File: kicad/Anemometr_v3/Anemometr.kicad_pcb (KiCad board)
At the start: 2 copper layers, 45 x 45 mm, 170 parts, among them J1 TxD, J10 +Z1, J11 +Z2, J12 +Z3, J13 +Z4, J14 -Z1, J15 -Z2, J16 -Z3, J17 -Z4, J18 1 TxD+, J19 2 TxD-, J2 RxD, J20 3 RxD+, J21 4-5, J22 6 RxD-, J23 7-8, J24 Conn_01x01_Female, J25 Conn_01x01_Female, J26 Conn_01x01_Female, J3 SCL, J4 SDA, J5 RST, J6 +EXT, J7 -EXT, J8 SWD, J9 SWC, Q1 5N10, U1 STM32F103C8Tx, U2 TS5A3166DBVR, U3 TS5A3166DBVR, U4 LMR14206, U5 TS5A3166DBVR, U6 NCP1117-3.3, U7 TS5A3166DBVR, U8 MCP1703-3.3, U9 MCP1703-3.3, Y1 CSTCE8M00G52A-R0, Y2 ECS-250-20-33

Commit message: изменено:      kicad/Anemometr_v3/Anemometr-cache.lib 	изменено:      kicad/Anemometr_v3/Anemometr.kicad_pcb 	изменено:      kicad/Anemometr_v3/Anemometr.kicad_pcb-bak 	изменено:      kicad/Anemometr_v3/Anemometr.sch 	изменено:      kicad/Anemometr_v3/Anemometr.sch-bak
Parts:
- removed C1, C17, C2, C21, C32, C5, C51, C52, C57, C59: 0.1uF, Capacitor_SMD:C_0402_1005Metric
- removed C18, C6: 10nF, Capacitor_SMD:C_0402_1005Metric
- removed C34, C40: 100nF, Capacitor_SMD:C_0402_1005Metric
- removed C41, C47: 1,5nF, Capacitor_SMD:C_0402_1005Metric
- removed C60, C61: 10uF, Capacitor_SMD:C_0805_2012Metric
- removed D19, D7: MAX4477, Package_SO:MSOP-8_3x3mm_P0.65mm
- removed D20, D21: TLV3501, Package_TO_SOT_SMD:SOT-23-6
- removed R13, R31: 20k, Resistor_SMD:R_0402_1005Metric
- removed R16, R25, R33, R46, R48, R50: 100k, Resistor_SMD:R_0402_1005Metric
- removed R17: 110k, Resistor_SMD:R_0402_1005Metric
- removed R20, R45: 1k, Resistor_SMD:R_0402_1005Metric
- removed R29, R47: 5.1k, Resistor_SMD:R_0402_1005Metric
- removed R37, R49: 10k, Resistor_SMD:R_0402_1005Metric
- removed R5, R51: 3k, Resistor_SMD:R_0402_1005Metric
- removed R6, R7, R8: 3k, Resistor_SMD:R_0603_1608Metric
- removed U2, U3, U5, U7: TS5A3166DBVR, Package_TO_SOT_SMD:SOT-23-5
- removed U8: MCP1703-3.3, Package_TO_SOT_SMD:SOT-23
- added J27: +Z1, My-library:SMD-CONN, F.Cu at (33.8, 64.5)
- added J28: +Z1, My-library:SMD-CONN, F.Cu at (42.7, 71.5)
- added J29: +Z1, My-library:SMD-CONN, F.Cu at (49.0, 71.5)
- added J30: +Z1, My-library:SMD-CONN, F.Cu at (44.8, 71.5)
- added J31: +Z1, My-library:SMD-CONN, F.Cu at (46.9, 71.5)
- added J32: +Z1, My-library:SMD-CONN, F.Cu at (50.0, 76.2)
- added J33: +Z1, My-library:SMD-CONN, F.Cu at (47.9, 76.2)
- added J34: +Z1, My-library:SMD-CONN, F.Cu at (45.8, 76.2)
- added J35: +Z1, My-library:SMD-CONN, F.Cu at (43.7, 76.2)
- added J36: +Z1, My-library:SMD-CONN, F.Cu at (31.8, 66.6)
- added J37: +Z1, My-library:SMD-CONN, F.Cu at (35.9, 66.6)
- added J38: +Z1, My-library:SMD-CONN, F.Cu at (37.9, 66.6)
- added J39: +Z1, My-library:SMD-CONN, F.Cu at (33.8, 66.6)
- C23, C55, D18, L2: moved to F.Cu
- C58: moved to B.Cu
- D11: value SD4932B -> U6119SA
- J24: value Conn_01x01_Female -> +Z1; footprint My-library:ConnMini -> My-library:SMD-CONN; moved to F.Cu
- J25, J26: value Conn_01x01_Female -> +Z1; footprint My-library:ConnMini -> My-library:SMD-CONN
- moved L2 31.1 mm to (51.9, 68.2), turned to 180 degrees
- moved C23 25.7 mm to (50.9, 65.8), turned to 180 degrees
- moved D18 25.3 mm to (44.0, 65.8)
- moved J10 20.4 mm to (48.4, 80.2)
- moved J11 15.9 mm to (46.4, 80.2)
- moved J24 12.8 mm to (37.8, 64.5), turned to 270 degrees
- moved J15 11.5 mm to (39.8, 71.6)
- moved J12 11.2 mm to (44.4, 80.2)
- moved J14 11.1 mm to (39.8, 76.0)
- moved J26 9.12 mm to (31.8, 64.5), turned to 270 degrees
- moved J25 8.73 mm to (35.8, 64.5)
- moved C55 7.17 mm to (29.4, 65.2), turned to 90 degrees
- moved J7 6.78 mm to (39.8, 73.8)
- moved J17 6.73 mm to (39.8, 78.2)
- moved R15 6.57 mm to (57.8, 70.8), turned to 270 degrees
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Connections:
- J24 pad 1: SInput -> +5VA
- J25 pad 1: Net-(C47-Pad2) -> +5VA
- J26 pad 1: Net-(C41-Pad2) -> +5VA
- U1 pad 10: SInput -> SIn
- U1 pad 19: Z1 -> Z1Sel
- U1 pad 2: Z3-4 -> (no net)
- U1 pad 20: Z2 -> Z2Sel
- U1 pad 3: Z1-2 -> (no net)
- U1 pad 39: Z3 -> Z3Sel
- U1 pad 40: Z4 -> Z4Sel
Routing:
- net SInput: track 53.4 -> 0.00 mm, vias 3 -> 0
- net GND: track 192.9 -> 139.8 mm, vias 23 -> 12
- net 6v: track 67.2 -> 27.6 mm, vias 3 -> 2
- net +5VA: track 54.6 -> 18.3 mm, vias 6 -> 0
- net Z2: track 33.9 -> 0.00 mm, vias 3 -> 0
- net Z3-4: track 32.1 -> 0.00 mm, vias 1 -> 0
- net /+Z1: track 35.2 -> 4.27 mm
- net Z1: track 30.0 -> 0.00 mm, vias 5 -> 0
- net /+Z2: track 36.2 -> 7.30 mm
- net Z1-2: track 24.9 -> 0.00 mm, vias 1 -> 0
- net Net-(C23-Pad2): track 35.3 -> 11.3 mm
- net +3.3VP: track 21.4 -> 0.00 mm, vias 2 -> 0
- net Z4: track 19.2 -> 0.00 mm, vias 3 -> 0
- net a: track 18.5 -> 0.00 mm, vias 2 -> 0
- net /+Z3: track 28.1 -> 10.7 mm
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
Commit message: изменено:      kicad/Anemometr_v3/Anemometr.kicad_pcb 	изменено:      kicad/Anemometr_v3/Anemometr.kicad_pcb-bak 	изменено:      stm32cubeide/Anemometr_v3/Anemometr_3.ioc 	изменено:      stm32cubeide/Anemometr_v3/Core/Inc/main.h 	изменено:      stm32cubeide/Anemometr_v3/Core/Src/main.c 	изменено:      stm32cubeide/Anemometr_v3/Core/Src/stm32f1xx_hal_msp.c 	изменено:      stm32cubeide/Anemometr_v3/Debug/Anemometr_3.bin 	изменено:      stm32cubeide/Anemometr_v3/Debug/Anemometr_3.elf 	изменено:      stm32cubeide/Anemometr_v3/Debug/Anemometr_3.list 	изменено:      stm32cubeide/Anemometr_v3/Debug/Anemometr_3.map 	изменено:      stm32cubeide/Anemometr_v3/Debug/Core/Src/BME280.o 	изменено:      stm32cubeide/Anemometr_v3/Debug/Core/Src/main.o 	изменено:      stm32cubeide/Anemometr_v3/Debug/Core/Src/main.su 	изменено:      stm32cubeide/Anemometr_v3/Debug/Core/Src/stm32f1xx_hal_msp.o 	изменено:      stm32cubeide/Anemometr_v3/Debug/Core/Src/stm32f1xx_it.o
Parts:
- moved C14 18.1 mm to (61.5, 69.5)
- moved C27 18.1 mm to (61.9, 79.4)
- moved C35 18.1 mm to (58.4, 79.4)
- moved C38 18.1 mm to (60.8, 79.4)
- moved C45 18.1 mm to (52.6, 76.5)
- moved C56 18.1 mm to (64.8, 66.7)
- moved D10 18.1 mm to (60.7, 79.7)
- moved D15 18.1 mm to (41.5, 70.2)
- moved J21 18.1 mm to (51.5, 72.2)
- moved L1 18.1 mm to (52.2, 77.6)
- moved R23 18.1 mm to (35.8, 81.3)
- moved R34 18.1 mm to (26.8, 83.0)
- moved C22 18.1 mm to (60.2, 50.5)
- moved C23 18.1 mm to (55.1, 48.3)
- moved C3 18.1 mm to (52.5, 49.2)
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
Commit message: изменено:      kicad/Anemometr_v3/Anemometr.kicad_pcb 	изменено:      kicad/Anemometr_v3/Anemometr.kicad_pcb-bak
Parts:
- moved U9 0.25 mm to (57.8, 51.9), turned to 90 degrees
- moved C36 0.23 mm to (65.2, 54.0)
- moved C9 0.11 mm to (55.5, 52.1)
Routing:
- net GND: track 139.8 -> 145.5 mm, vias 12 -> 13
- net +3V3: track 38.1 -> 37.3 mm

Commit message: изменено:      kicad/Anemometr_v3/Anemometr.kicad_pcb 	изменено:      kicad/Anemometr_v3/Anemometr.kicad_pcb-bak 	изменено:      kicad/Anemometr_v3/Anemometr.sch 	изменено:      kicad/Anemometr_v3/Anemometr.sch-bak
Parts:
- D17: value SS56 -> SS56, VS10MQ060-M3/5
- R15: footprint Resistor_SMD:R_0603_1608Metric -> Resistor_SMD:R_0402_1005Metric
- moved D5 0.51 mm to (62.1, 50.9)
- moved R15 0.07 mm to (62.1, 53.3)
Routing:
- net Z4Sel: track 3.70 -> 2.55 mm
- net GND: vias 13 -> 14

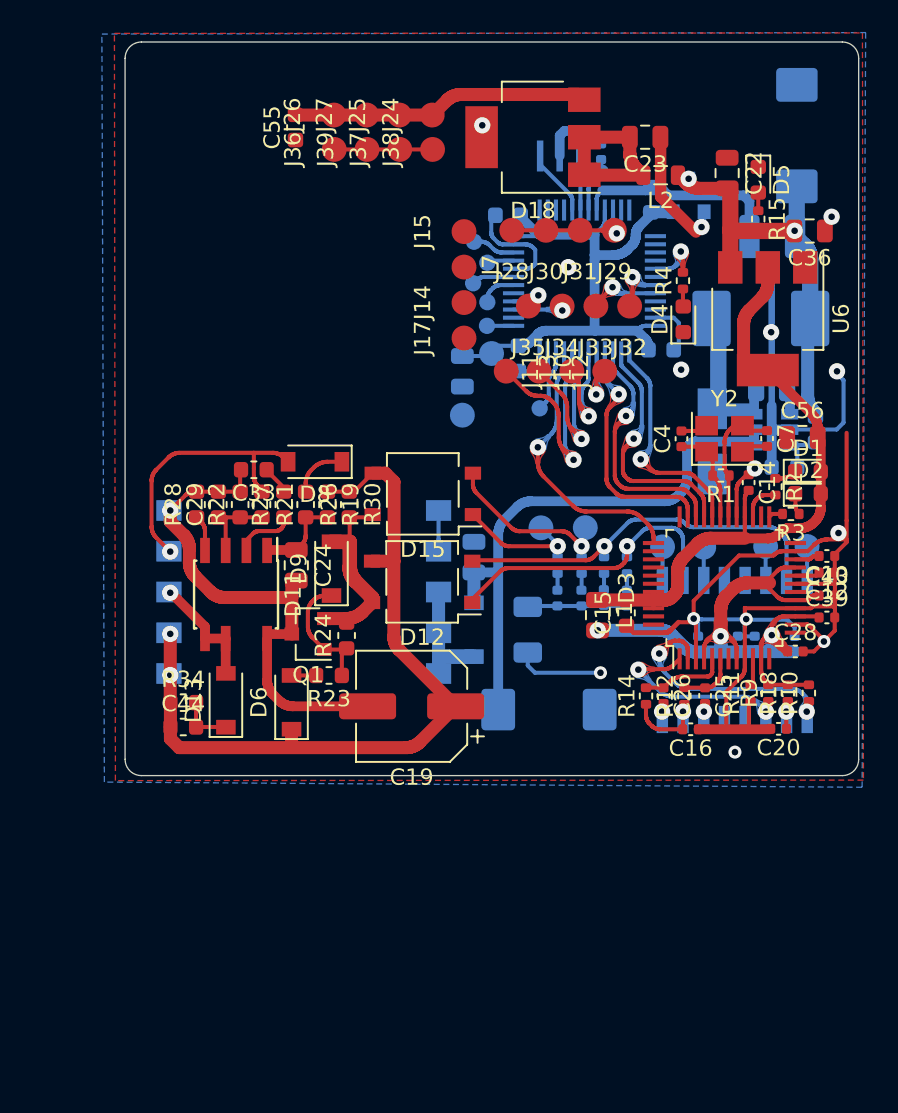
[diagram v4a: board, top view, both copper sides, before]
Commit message: изменено:      kicad/Anemometr_v3/Anemometr-cache.lib 	изменено:      kicad/Anemometr_v3/Anemometr.kicad_pcb 	изменено:      kicad/Anemometr_v3/Anemometr.kicad_pcb-bak 	изменено:      kicad/Anemometr_v3/Anemometr.sch 	изменено:      kicad/Anemometr_v3/Anemometr.sch-bak 	изменено:      kicad/Anemometr_v3/fp-info-cache
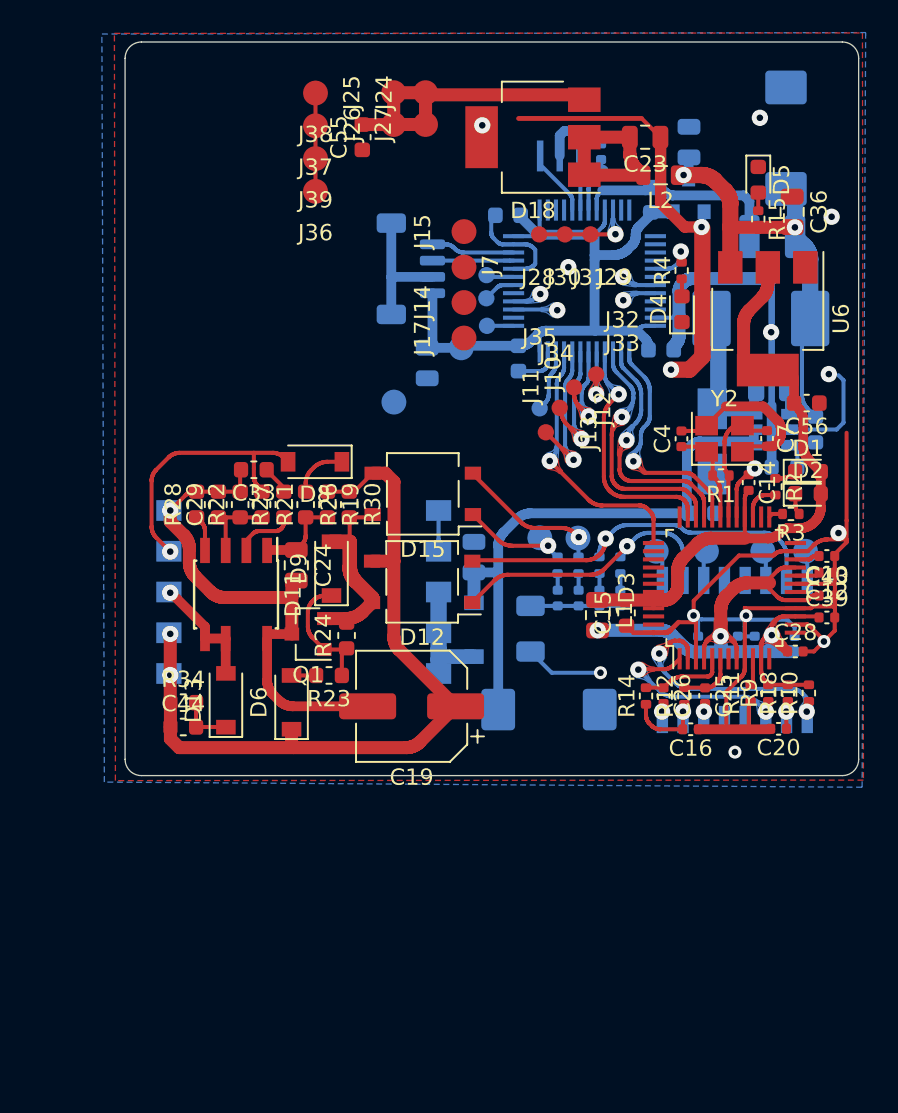
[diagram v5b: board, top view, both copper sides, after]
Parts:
- removed J4: SDA, My-library:ConnMini
- added C1: 2.2uF, Capacitor_SMD:C_0603_1608Metric, B.Cu at (58.6, 71.4)
- C22: moved to B.Cu
- C56: footprint Capacitor_SMD:C_0805_2012Metric -> Capacitor_SMD:C_0603_1608Metric
- J10, J11, J12, J13, J28, J29, J30, J31, J32, J33, J34, J35: footprint My-library:SMD-CONN -> My-library:ConnMini
- J3: value SCL -> Conn_01x04_MountingPin; footprint My-library:ConnMini -> Connector_JST:JST_SH_BM04B-SRSS-TB_1x04-1MP_P1.00mm_Vertical
- moved J38 7.97 mm to (34.9, 45.6), turned to 0 degrees
- moved J37 5.37 mm to (34.9, 47.6), turned to 0 degrees
- moved J3 4.70 mm to (40.8, 56.4), turned to 270 degrees
- moved J13 4.47 mm to (49.1, 66.4)
- moved J16 4.28 mm to (39.7, 64.5)
- moved C55 4.14 mm to (37.8, 48.3)
- moved J26 3.72 mm to (39.7, 47.5)
- moved J27 3.66 mm to (41.6, 47.5)
- moved J39 3.21 mm to (34.9, 49.6), turned to 0 degrees
- moved C22 3.01 mm to (57.8, 48.6)
- moved J36 2.82 mm to (34.9, 51.6), turned to 0 degrees
- moved J12 2.58 mm to (49.9, 64.9)
- moved C37 2.22 mm to (41.8, 62.1)
- moved C56 2.13 mm to (65.1, 64.6), turned to 180 degrees
- moved J6 1.89 mm to (43.9, 61.2)
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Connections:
- J3 pad 1: /SCL -> /SDA
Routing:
- net GND: track 145.5 -> 188.3 mm, vias 14 -> 15
- net +3V3: track 37.3 -> 42.7 mm
- net /+Z4: track 14.4 -> 9.32 mm
- net /SCL: track 1.66 -> 4.98 mm
- net /+Z3: track 10.7 -> 8.02 mm
- net /SDA: track 2.64 -> 5.12 mm
- net Net-(D15-Pad2): track 11.2 -> 8.86 mm
- net Z2Sel: track 4.33 -> 2.10 mm
- net SIn: track 8.51 -> 6.40 mm
- net Net-(D15-Pad1): track 8.36 -> 7.00 mm
- net Z1Sel: track 3.43 -> 2.14 mm
- net Net-(D10-Pad10): track 18.9 -> 17.8 mm
- net /+Z2: track 7.30 -> 6.30 mm
- net /RxD: track 2.61 -> 1.71 mm
- net +5VA: track 18.3 -> 19.2 mm
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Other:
- board text added: "1"
- board text added: "2"
- board text added: "3"
- board text added: "3.3v"
- board text added: "45"
- board text added: "6"
- board text added: "78"
- board text added: "GND"
- board text added: "RST"
- board text added: "RxD"
- board text added: "SCL"
- board text added: "SDA"
- board text added: "SWC"
- board text added: "SWD"
- board text added: "TxD"

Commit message: изменено:      kicad/Anemometr_v3/Anemometr-cache.lib 	изменено:      kicad/Anemometr_v3/Anemometr.kicad_pcb 	изменено:      kicad/Anemometr_v3/Anemometr.kicad_pcb-bak 	изменено:      kicad/Anemometr_v3/Anemometr.sch 	изменено:      kicad/Anemometr_v3/Anemometr.sch-bak 	изменено:      kicad/Anemometr_v3/fp-info-cache
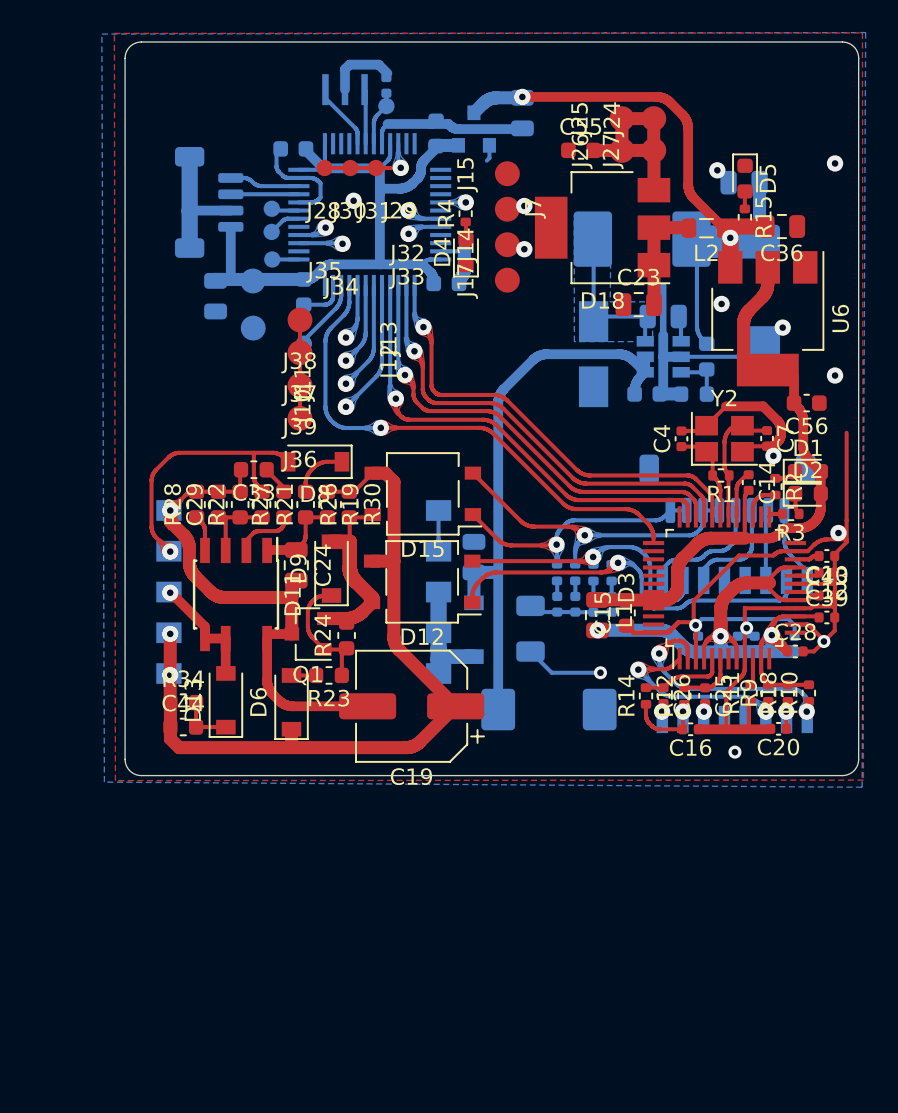
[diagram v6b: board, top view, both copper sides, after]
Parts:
- removed J18: 1 TxD+, My-library:SMD-CONN
- removed J19: 2 TxD-, My-library:SMD-CONN
- removed J20: 3 RxD+, My-library:SMD-CONN
- removed J21: 4-5, My-library:SMD-CONN
- removed J22: 6 RxD-, My-library:SMD-CONN
- removed J23: 7-8, My-library:SMD-CONN
- added J4: JST-SH1.0, Connector_JST:JST_SH_BM08B-SRSS-TB_1x08-1MP_P1.00mm_Vertical, B.Cu at (60.2, 69.9)
- C54: footprint Capacitor_SMD:C_1210_3225Metric -> Capacitor_SMD:C_0805_2012Metric
- D11: value U6119SA -> ?U6119SA?
- D14: value T4932B -> ?T4932B?
- J3: value Conn_01x04_MountingPin -> JST-SH1.0
- moved J10 15.5 mm to (36.8, 64.8)
- moved J8 15.0 mm to (34.2, 61.0)
- moved J24 14.1 mm to (55.7, 47.1)
- moved J25 14.1 mm to (53.7, 47.1)
- moved J26 14.1 mm to (53.7, 49.1)
- moved J27 14.1 mm to (55.6, 49.1)
- moved J11 14.0 mm to (36.8, 63.4)
- moved J36 14.0 mm to (34.0, 65.5)
- moved J38 14.0 mm to (34.0, 59.5)
- moved J39 14.0 mm to (34.0, 63.5)
- moved J37 14.0 mm to (34.0, 61.5)
- moved C11 13.8 mm to (33.6, 49.0)
- moved C13 13.8 mm to (34.2, 57.8)
- moved C3 13.8 mm to (39.3, 45.1)
- moved C8 13.8 mm to (43.0, 57.3)
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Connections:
- net Net-(D15-Pad1) renamed /7-8
- net Net-(D15-Pad2) renamed /4-5
- D10 pad 11: Net-(D10-Pad11) -> /RxD+
- D10 pad 14: Net-(D10-Pad14) -> /TxD-
- D10 pad 16: Net-(D10-Pad16) -> /TxD+
- D10 pad 9: Net-(D10-Pad9) -> /RxD-
- D12 pad 1: Net-(D10-Pad10) -> Net-(D10-Pad15)
- D12 pad 2: Net-(D10-Pad15) -> Net-(D10-Pad10)
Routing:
- net GND: track 188.3 -> 145.9 mm
- net nrst: track 16.3 -> 32.0 mm
- net mosi: track 15.1 -> 28.7 mm
- net scsn: track 14.5 -> 27.7 mm
- net 6v: track 27.9 -> 40.8 mm
- net sclk: track 15.2 -> 27.8 mm
- net miso: track 15.4 -> 27.9 mm
- net /4-5: track 8.86 -> 19.7 mm
- net /7-8: track 7.00 -> 16.3 mm
- net /RxD-: track 0.00 -> 7.61 mm
- net +5VA: track 19.2 -> 12.0 mm
- net /RxD+: track 0.00 -> 6.53 mm
- net /+Z4: track 9.32 -> 3.43 mm
- net /TxD+: track 0.00 -> 4.82 mm
- net /+Z1: track 3.85 -> 8.30 mm
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- added copper zone on B.Cu, net Net-(C53-Pad1)
- added copper zone on F.Cu, net Net-(D10-Pad15)
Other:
- board text added: "4"
- board text added: "5"
- board text added: "7"
- board text added: "8"
- board text removed: "45"
- board text removed: "78"
